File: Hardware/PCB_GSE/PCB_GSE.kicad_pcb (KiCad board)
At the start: 4 copper layers, 74 x 95.6 mm, 155 parts, among them J1 Conn_01x02, J2 BM03B-GHS-TBT, J3 GT17HN-4DP-2H(D)(56), J4 Conn_01x06_Pin, J5 Screw_Terminal_01x04, J6 Screw_Terminal_01x04, J7 Screw_Terminal_01x04, J8 Vin_XT30PW-F, U1 MAX6612MXK, U10 MP28167GQ-B-P, U2 ISOW1044, U3 SI5442DU-T1-GE3, U4 INA125UA/2K5, U5 STM32F103CBT6, U6 SI5442DU-T1-GE3, U7 SI5442DU-T1-GE3, U8 MPQ9843GLE-5-AEC1-Z, U9 TLV75733PDBVR, Y1 830050510

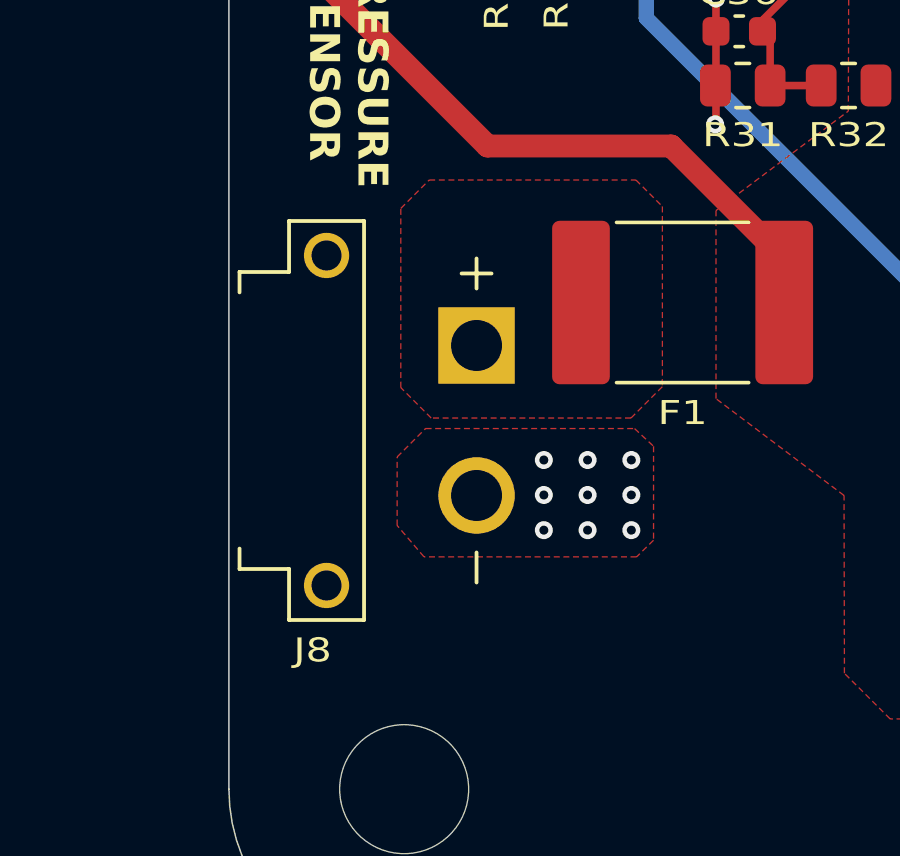
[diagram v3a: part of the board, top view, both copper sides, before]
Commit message: fix(moteur + gse): move xt30 to border + fix silkscreen + connect shield to gnd  in pressure sensor + remake rounded corners + fix/add doc
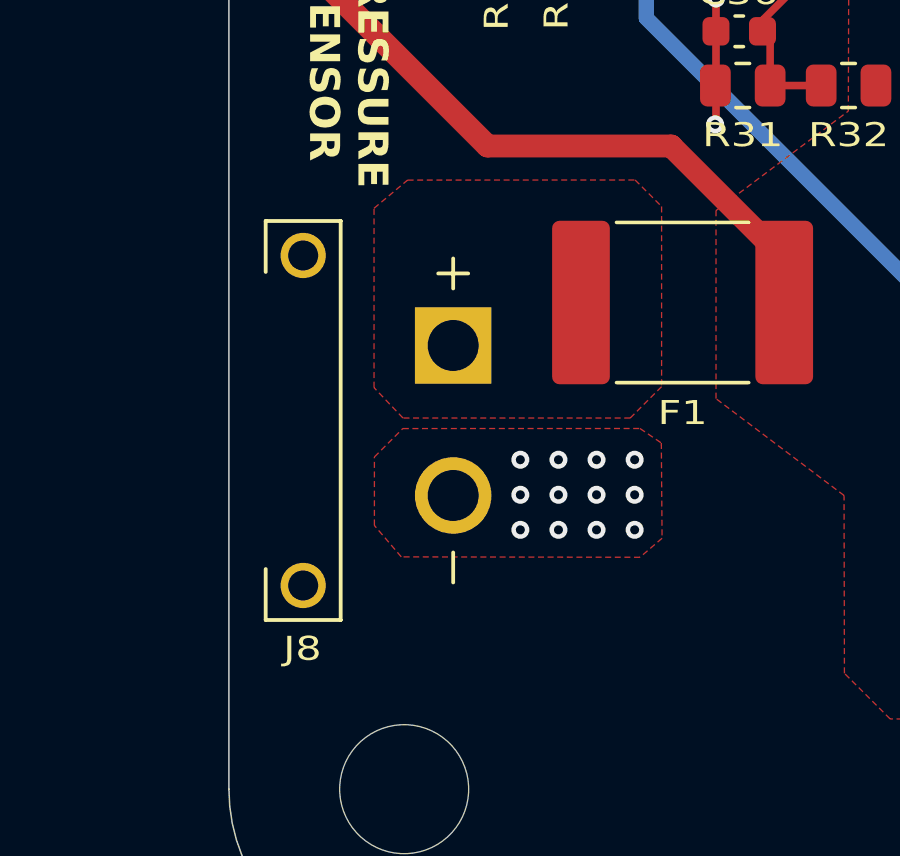
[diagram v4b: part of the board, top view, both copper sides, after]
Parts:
- moved J8 0.78 mm to (117.2, 131.0)
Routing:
- net GND: vias 229 -> 232
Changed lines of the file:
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@@
 	(footprint "pcb_moteur:XT30PW-F"
 		(layer "F.Cu")
-		(at 118 131 90)
+		(at 117.221 131 90)
 		(property "Reference" "J8"
-			(at -7.659658 -0.465457 180)
+			(at -7.6078 -0.0254 180)
 			(layer "F.SilkS")
 			(effects
@@
 		(attr through_hole)
 		(fp_line
-			(start 4.95 -2.9)
-			(end 4.27 -2.9)
-			(stroke
-				(width 0.127)
-				(type solid)
-			)
-			(layer "F.SilkS")
-		)
-		(fp_line
-			(start -4.95 -2.9)
-			(end -4.27 -2.9)
-			(stroke
-				(width 0.127)
-				(type solid)
-			)
-			(layer "F.SilkS")
-		)
-		(fp_line
 			(start 6.65 -1.25)
 			(end 4.95 -1.25)
@@
 		)
 		(fp_line
-			(start 4.95 -1.25)
-			(end 4.95 -2.9)
-			(stroke
-				(width 0.127)
-				(type solid)
-			)
-			(layer "F.SilkS")
-		)
-		(fp_line
-			(start -4.95 -1.25)
-			(end -4.95 -2.9)
-			(stroke
-				(width 0.127)
-				(type solid)
-			)
-			(layer "F.SilkS")
-		)
-		(fp_line
 			(start -6.65 -1.25)
 			(end -4.95 -1.25)
@@
 		)
 		(fp_line
-			(start 4.95 -2.9)
-			(end 4.27 -2.9)
-			(stroke
-				(width 0.127)
-				(type solid)
-			)
-			(layer "F.Fab")
-		)
-		(fp_line
-			(start -4.95 -2.9)
-			(end -4.27 -2.9)
-			(stroke
-				(width 0.127)
-				(type solid)
-			)
-			(layer "F.Fab")
-		)
-		(fp_line
 			(start 6.65 -1.25)
 			(end 4.95 -1.25)
@@
 		)
 		(fp_line
-			(start 4.95 -1.25)
-			(end 4.95 -2.9)
-			(stroke
-				(width 0.127)
-				(type solid)
-			)
-			(layer "F.Fab")
-		)
-		(fp_line
-			(start -4.95 -1.25)
-			(end -4.95 -2.9)
-			(stroke
-				(width 0.127)
-				(type solid)
-			)
-			(layer "F.Fab")
-		)
-		(fp_line
 			(start -6.65 -1.25)
 			(end -4.95 -1.25)
@@
 	)
 	(via
-		(at 125.243463 132.317819)
+		(at 124.46 132.3086)
 		(size 0.6)
 		(drill 0.3)
@@
 	)
 	(via
+		(at 128.27 133.477)
+		(size 0.6)
+		(drill 0.3)
+		(layers "F.Cu" "B.Cu")
+		(free yes)
+		(net 46)
+	)
+	(via
 		(at 145.966276 112.135759)
 		(size 0.6)
@@
 	)
 	(via
-		(at 128.159508 133.483491)
+		(at 127 133.477)
 		(size 0.6)
 		(drill 0.3)
@@
 	)
 	(via
+		(at 128.27 132.3086)
+		(size 0.6)
+		(drill 0.3)
+		(layers "F.Cu" "B.Cu")
+		(free yes)
+		(net 46)
+	)
+	(via
 		(at 159.228257 126.957148)
 		(size 0.6)
@@
 	)
 	(via
-		(at 128.159508 132.317819)
+		(at 127 132.3086)
 		(size 0.6)
 		(drill 0.3)
@@
 	)
 	(via
-		(at 125.243463 134.655695)
+		(at 124.46 134.6454)
 		(size 0.6)
 		(drill 0.3)
@@
 	)
 	(via
-		(at 126.701486 134.655695)
+		(at 125.73 134.6454)
 		(size 0.6)
 		(drill 0.3)
@@
 	)
 	(via
-		(at 128.159508 134.655695)
+		(at 127 134.6454)
 		(size 0.6)
 		(drill 0.3)
@@
 	)
 	(via
+		(at 128.27 134.6454)
+		(size 0.6)
+		(drill 0.3)
+		(layers "F.Cu" "B.Cu")
+		(free yes)
+		(net 46)
+	)
+	(via
 		(at 174.407039 130.254257)
 		(size 0.6)
@@
 	)
 	(via
-		(at 125.243463 133.483491)
+		(at 124.46 133.477)
 		(size 0.6)
 		(drill 0.3)
@@
 	)
 	(via
-		(at 126.701486 132.317819)
+		(at 125.73 132.3086)
 		(size 0.6)
 		(drill 0.3)
@@
 	)
 	(via
-		(at 126.701486 133.483491)
+		(at 125.73 133.477)
 		(size 0.6)
 		(drill 0.3)
@@
 		(polygon
 			(pts
-				(xy 121.487597 130.918328) (xy 120.475392 129.906123) (xy 120.475392 123.93085) (xy 121.422293 122.983949)
-				(xy 128.311815 122.983949) (xy 129.193413 123.865547) (xy 129.193413 129.873471) (xy 128.148556 130.918328)
+				(xy 120.5484 130.918328) (xy 119.5832 129.906123) (xy 119.5832 123.9266) (xy 120.7008 122.9868)
+				(xy 128.286415 122.983949) (xy 129.168013 123.865547) (xy 129.168013 129.873471) (xy 128.123156 130.918328)
 			)
 		)
@@
 		(polygon
 			(pts
-				(xy 121.25 135.546716) (xy 120.352948 134.5) (xy 120.352948 132.216235) (xy 121.299849 131.269334)
-				(xy 128.266805 131.269334) (xy 128.900038 131.859277) (xy 128.900038 134.991467) (xy 128.334404 135.546716)
+				(xy 120.491937 135.546716) (xy 119.594885 134.5) (xy 119.594885 132.216235) (xy 120.541786 131.269334)
+				(xy 128.4478 131.2672) (xy 129.159 131.7498) (xy 129.1844 134.9248) (xy 128.4478 135.5598)
 			)
 		)
